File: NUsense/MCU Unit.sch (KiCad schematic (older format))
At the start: 45 parts, among them SW301 SW_Push, U301 STM32F746ZGT6, X301 24MHz, X302 ST3215SB32768H5

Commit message: pwm
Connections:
- net GPIO_9: now also U301.128 (PG13); no longer U301.124 (PG9)
- net MPU_INT: now also U301.12 (PF2); no longer U301.139 (PB8)
- net MPU_SCL: now also U301.10 (PF0); no longer U301.136 (PB6)
- net MPU_SDA/SDI: now also U301.11 (PF1); no longer U301.137 (PB7)
- net USART1_RX: now also U301.137 (PB7); no longer U301.102 (PA10)
- net USART1_TX: now also U301.136 (PB6); no longer U301.101 (PA9)
- net USART6_EN: now also U301.118 (PD4); no longer U301.98 (PC8)
- net USART6_RX: now also U301.124 (PG9); no longer U301.97 (PC7)
- net USART6_TX: now also U301.129 (PG14); no longer U301.96 (PC6)
- net TIM1_CH1: now reaches U301.100 (PA8)
- new net TIM1_CH2: U301.101 (PA9)
- new net TIM1_CH3: U301.102 (PA10)
- new net TIM8_CH1: U301.96 (PC6)
- new net TIM8_CH2: U301.97 (PC7)
- new net TIM8_CH3: U301.98 (PC8)
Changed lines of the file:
@@
 	0    -1   -1   0
 $EndComp
-Text HLabel 5150 4800 0    60   Input ~ 0
+Text HLabel 12300 5900 0    60   Input ~ 0
 MPU_INT
-Text HLabel 5150 4700 0    60   Input ~ 0
+Text HLabel 12300 5800 0    60   Input ~ 0
 MPU_SDA/SDI
-Text HLabel 5150 4600 0    60   Input ~ 0
+Text HLabel 12300 5700 0    60   Input ~ 0
 MPU_SCL
 Text HLabel 3250 7700 0    60   Input ~ 0
@@
 Text HLabel 5150 3600 0    60   BiDi ~ 0
 JTMS_SWDIO
-Text HLabel 5150 3200 0    60   Output ~ 0
+Text HLabel 5150 4600 0    60   Output ~ 0
 USART1_TX
-Text HLabel 5150 3300 0    60   Input ~ 0
+Text HLabel 5150 4700 0    60   Input ~ 0
 USART1_RX
-Text HLabel 6650 2900 2    60   Output ~ 0
+Text HLabel 13800 3700 2    60   Output ~ 0
 USART6_TX
-Text HLabel 6650 3000 2    60   Input ~ 0
+Text HLabel 13800 3200 2    60   Input ~ 0
 USART6_RX
 Text HLabel 6650 3400 2    60   Input ~ 0
@@
 Text HLabel 12300 3400 0    60   BiDi ~ 0
 VS_ALERT
-Text HLabel 6650 3100 2    60   Output ~ 0
+Text HLabel 12300 2700 0    60   Output ~ 0
 USART6_EN
 Text HLabel 12300 3000 0    60   Output ~ 0
@@
 Text HLabel 13800 3100 2    60   BiDi ~ 0
 GPIO_8
-Text HLabel 13800 3200 2    60   BiDi ~ 0
+Text HLabel 13800 3600 2    60   BiDi ~ 0
 GPIO_9
 Text HLabel 13800 3300 2    60   BiDi ~ 0
@@
 Text HLabel 13800 3500 2    60   BiDi ~ 0
 GPIO_12
+Text HLabel 5150 3100 0    60   Output ~ 0
+TIM1_CH1
+Text HLabel 5150 3200 0    60   Output ~ 0
+TIM1_CH2
+Text HLabel 5150 3300 0    60   Output ~ 0
+TIM1_CH3
+Text HLabel 6650 2900 2    60   Output ~ 0
+TIM8_CH1
+Text HLabel 6650 3000 2    60   Output ~ 0
+TIM8_CH2
+Text HLabel 6650 3100 2    60   Output ~ 0
+TIM8_CH3
 $EndSCHEMATC

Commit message: Cleans up some minor things
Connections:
- net labels added: USB_DATA
- net labels removed: OTG_HS_ULPI_D
- wire segments 141 -> 149
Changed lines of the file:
@@
 $EndComp
 $Comp
-L GND #PWR14
+L GND #PWR306
 U 1 1 5A6BFE16
 P 4000 6200
-F 0 "#PWR14" H 4000 5950 50  0001 C CNN
+F 0 "#PWR306" H 4000 5950 50  0001 C CNN
 F 1 "GND" H 4000 6050 50  0000 C CNN
 F 2 "" H 4000 6200 50  0001 C CNN
@@
 $EndComp
 $Comp
-L GND #PWR11
+L GND #PWR303
 U 1 1 5A6BFE38
 P 3200 6950
-F 0 "#PWR11" H 3200 6700 50  0001 C CNN
+F 0 "#PWR303" H 3200 6700 50  0001 C CNN
 F 1 "GND" H 3200 6800 50  0000 C CNN
 F 2 "" H 3200 6950 50  0001 C CNN
@@
 $EndComp
 $Comp
-L GND #PWR13
+L GND #PWR305
 U 1 1 5A6BFE45
 P 3800 7150
-F 0 "#PWR13" H 3800 6900 50  0001 C CNN
+F 0 "#PWR305" H 3800 6900 50  0001 C CNN
 F 1 "GND" H 3800 7000 50  0000 C CNN
 F 2 "" H 3800 7150 50  0001 C CNN
@@
 $EndComp
 $Comp
-L GND #PWR9
+L GND #PWR301
 U 1 1 5A6BFE4B
 P 2650 7150
-F 0 "#PWR9" H 2650 6900 50  0001 C CNN
+F 0 "#PWR301" H 2650 6900 50  0001 C CNN
 F 1 "GND" H 2650 7000 50  0000 C CNN
 F 2 "" H 2650 7150 50  0001 C CNN
@@
 $EndComp
 $Comp
-L GND #PWR16
+L GND #PWR308
 U 1 1 5A6BFE84
 P 4950 8100
-F 0 "#PWR16" H 4950 7850 50  0001 C CNN
+F 0 "#PWR308" H 4950 7850 50  0001 C CNN
 F 1 "GND" H 4950 7950 50  0000 C CNN
 F 2 "" H 4950 8100 50  0001 C CNN
@@
 $EndComp
 $Comp
-L GND #PWR21
+L GND #PWR313
 U 1 1 5A6BFE8A
 P 6700 7300
-F 0 "#PWR21" H 6700 7050 50  0001 C CNN
+F 0 "#PWR313" H 6700 7050 50  0001 C CNN
 F 1 "GND" H 6700 7150 50  0000 C CNN
 F 2 "" H 6700 7300 50  0001 C CNN
@@
 $EndComp
 $Comp
-L GND #PWR26
+L GND #PWR318
 U 1 1 5A6BFEA7
 P 8750 9450
-F 0 "#PWR26" H 8750 9200 50  0001 C CNN
+F 0 "#PWR318" H 8750 9200 50  0001 C CNN
 F 1 "GND" H 8750 9300 50  0000 C CNN
 F 2 "" H 8750 9450 50  0001 C CNN
@@
 $EndComp
 $Comp
-L GND #PWR23
+L GND #PWR315
 U 1 1 5A6BFEDA
 P 8050 10650
-F 0 "#PWR23" H 8050 10400 50  0001 C CNN
+F 0 "#PWR315" H 8050 10400 50  0001 C CNN
 F 1 "GND" H 8050 10500 50  0000 C CNN
 F 2 "" H 8050 10650 50  0001 C CNN
@@
 $EndComp
 $Comp
-L GND #PWR25
+L GND #PWR317
 U 1 1 5A6BFEE0
 P 8400 10650
-F 0 "#PWR25" H 8400 10400 50  0001 C CNN
+F 0 "#PWR317" H 8400 10400 50  0001 C CNN
 F 1 "GND" H 8400 10500 50  0000 C CNN
 F 2 "" H 8400 10650 50  0001 C CNN
@@
 $EndComp
 $Comp
-L GND #PWR27
+L GND #PWR319
 U 1 1 5A6BFEE6
 P 8750 10650
-F 0 "#PWR27" H 8750 10400 50  0001 C CNN
+F 0 "#PWR319" H 8750 10400 50  0001 C CNN
 F 1 "GND" H 8750 10500 50  0000 C CNN
 F 2 "" H 8750 10650 50  0001 C CNN
@@
 $EndComp
 $Comp
-L GND #PWR28
+L GND #PWR320
 U 1 1 5A6BFEEC
 P 9050 10650
-F 0 "#PWR28" H 9050 10400 50  0001 C CNN
+F 0 "#PWR320" H 9050 10400 50  0001 C CNN
 F 1 "GND" H 9050 10500 50  0000 C CNN
 F 2 "" H 9050 10650 50  0001 C CNN
@@
 $EndComp
 $Comp
-L GND #PWR29
+L GND #PWR321
 U 1 1 5A6BFEF3
 P 11000 9500
-F 0 "#PWR29" H 11000 9250 50  0001 C CNN
+F 0 "#PWR321" H 11000 9250 50  0001 C CNN
 F 1 "GND" H 11000 9350 50  0000 C CNN
 F 2 "" H 11000 9500 50  0001 C CNN
@@
 $EndComp
 $Comp
-L GND #PWR30
+L GND #PWR322
 U 1 1 5A6BFF00
 P 11000 10500
-F 0 "#PWR30" H 11000 10250 50  0001 C CNN
+F 0 "#PWR322" H 11000 10250 50  0001 C CNN
 F 1 "GND" H 11000 10350 50  0000 C CNN
 F 2 "" H 11000 10500 50  0001 C CNN
@@
 $EndComp
 $Comp
-L GND #PWR31
+L GND #PWR323
 U 1 1 5A6BFF06
 P 11300 10500
-F 0 "#PWR31" H 11300 10250 50  0001 C CNN
+F 0 "#PWR323" H 11300 10250 50  0001 C CNN
 F 1 "GND" H 11300 10350 50  0000 C CNN
 F 2 "" H 11300 10500 50  0001 C CNN
@@
 $EndComp
 $Comp
-L GND #PWR15
+L GND #PWR307
 U 1 1 5A6BFF68
 P 4550 10350
-F 0 "#PWR15" H 4550 10100 50  0001 C CNN
+F 0 "#PWR307" H 4550 10100 50  0001 C CNN
 F 1 "GND" H 4550 10200 50  0000 C CNN
 F 2 "" H 4550 10350 50  0001 C CNN
@@
 Wire Wire Line
 	11300 9900 11300 10100
-Text GLabel 5150 2600 0    60   Input ~ 0
-OTG_HS_ULPI_D
-Text GLabel 5150 4000 0    60   Input ~ 0
-OTG_HS_ULPI_D
-Text GLabel 5150 4100 0    60   Input ~ 0
-OTG_HS_ULPI_D
-Text GLabel 5150 4500 0    60   Input ~ 0
-OTG_HS_ULPI_D
-Text GLabel 5150 5000 0    60   Input ~ 0
-OTG_HS_ULPI_D
-Text GLabel 5150 5100 0    60   Input ~ 0
-OTG_HS_ULPI_D
-Text GLabel 5150 5200 0    60   Input ~ 0
-OTG_HS_ULPI_D
-Text GLabel 5150 5300 0    60   Input ~ 0
-OTG_HS_ULPI_D
-$Comp
-L +3.3V #PWR20
+$Comp
+L +3.3V #PWR312
 U 1 1 5A6FCDF0
 P 6700 7000
-F 0 "#PWR20" H 6700 6850 50  0001 C CNN
+F 0 "#PWR312" H 6700 6850 50  0001 C CNN
 F 1 "+3.3V" H 6700 7140 50  0000 C CNN
 F 2 "" H 6700 7000 50  0001 C CNN
@@
 $EndComp
 $Comp
-L +3.3V #PWR18
+L +3.3V #PWR310
 U 1 1 5A6FCE7A
 P 5800 7500
-F 0 "#PWR18" H 5800 7350 50  0001 C CNN
+F 0 "#PWR310" H 5800 7350 50  0001 C CNN
 F 1 "+3.3V" H 5800 7640 50  0000 C CNN
 F 2 "" H 5800 7500 50  0001 C CNN
@@
 $EndComp
 $Comp
-L +3.3V #PWR24
+L +3.3V #PWR316
 U 1 1 5A6FD2DC
 P 8250 8400
-F 0 "#PWR24" H 8250 8250 50  0001 C CNN
+F 0 "#PWR316" H 8250 8250 50  0001 C CNN
 F 1 "+3.3V" H 8250 8540 50  0000 C CNN
 F 2 "" H 8250 8400 50  0001 C CNN
@@
 VDD3o3V_MCU
 $Comp
-L GND #PWR17
+L GND #PWR309
 U 1 1 5A701246
 P 5500 9800
-F 0 "#PWR17" H 5500 9550 50  0001 C CNN
+F 0 "#PWR309" H 5500 9550 50  0001 C CNN
 F 1 "GND" H 5500 9650 50  0000 C CNN
 F 2 "" H 5500 9800 50  0001 C CNN
@@
 VDD_REF+
 $Comp
-L GND #PWR19
+L GND #PWR311
 U 1 1 5A7014A6
 P 6300 10750
-F 0 "#PWR19" H 6300 10500 50  0001 C CNN
+F 0 "#PWR311" H 6300 10500 50  0001 C CNN
 F 1 "GND" H 6300 10600 50  0000 C CNN
 F 2 "" H 6300 10750 50  0001 C CNN
@@
 	8400 9650 8400 10300
 $Comp
-L +3.3V #PWR22
+L +3.3V #PWR314
 U 1 1 5A6FD08D
 P 6900 9900
-F 0 "#PWR22" H 6900 9750 50  0001 C CNN
+F 0 "#PWR314" H 6900 9750 50  0001 C CNN
 F 1 "+3.3V" H 6900 10040 50  0000 C CNN
 F 2 "" H 6900 9900 50  0001 C CNN
@@
 $EndComp
 $Comp
-L GND #PWR10
+L GND #PWR302
 U 1 1 5A6BFE10
 P 2700 6200
-F 0 "#PWR10" H 2700 5950 50  0001 C CNN
+F 0 "#PWR302" H 2700 5950 50  0001 C CNN
 F 1 "GND" H 2700 6050 50  0000 C CNN
 F 2 "" H 2700 6200 50  0001 C CNN
@@
 	5150 5800 4600 5800
 $Comp
-L GND #PWR12
+L GND #PWR304
 U 1 1 5A7647F9
 P 3400 6450
-F 0 "#PWR12" H 3400 6200 50  0001 C CNN
+F 0 "#PWR304" H 3400 6200 50  0001 C CNN
 F 1 "GND" H 3400 6300 50  0000 C CNN
 F 2 "" H 3400 6450 50  0001 C CNN
@@
 Text HLabel 6650 3100 2    60   Output ~ 0
 TIM8_CH3
+Entry Bus Bus
+	4200 2500 4300 2600
+Entry Bus Bus
+	4200 3900 4300 4000
+Entry Bus Bus
+	4200 4000 4300 4100
+Entry Bus Bus
+	4200 4400 4300 4500
+Entry Bus Bus
+	4200 4900 4300 5000
+Entry Bus Bus
+	4200 5000 4300 5100
+Entry Bus Bus
+	4200 5100 4300 5200
+Entry Bus Bus
+	4200 5200 4300 5300
+Wire Bus Line
+	4200 5200 4200 2400
+Wire Bus Line
+	4200 2400 3950 2400
+Text HLabel 3950 2400 0    60   BiDi ~ 0
+USB_DATA
+Wire Wire Line
+	5150 5300 4300 5300
+Wire Wire Line
+	5150 5200 4300 5200
+Wire Wire Line
+	5150 5100 4300 5100
+Wire Wire Line
+	5150 5000 4300 5000
+Wire Wire Line
+	5150 4500 4300 4500
+Wire Wire Line
+	5150 4100 4300 4100
+Wire Wire Line
+	5150 4000 4300 4000
+Wire Wire Line
+	4300 2600 5150 2600
 $EndSCHEMATC

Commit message: Further Cleaning
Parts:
- added C335: 0.1uF, Capacitors_SMD:C_0805_HandSoldering, symbol C
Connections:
- net labels removed: RTC_BAT, VDD3o3V_MCU, VDD_REF+
- wire segments 149 -> 152
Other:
- note added: "RTC Battery Input"
- moved on the sheet: C324, C325, C326, C327

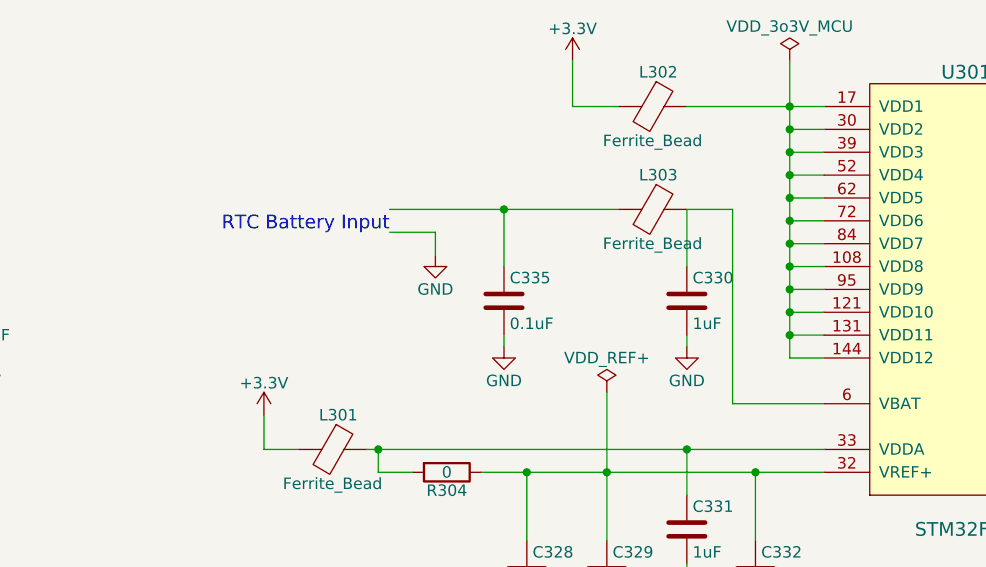
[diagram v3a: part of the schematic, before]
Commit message: RTC removed
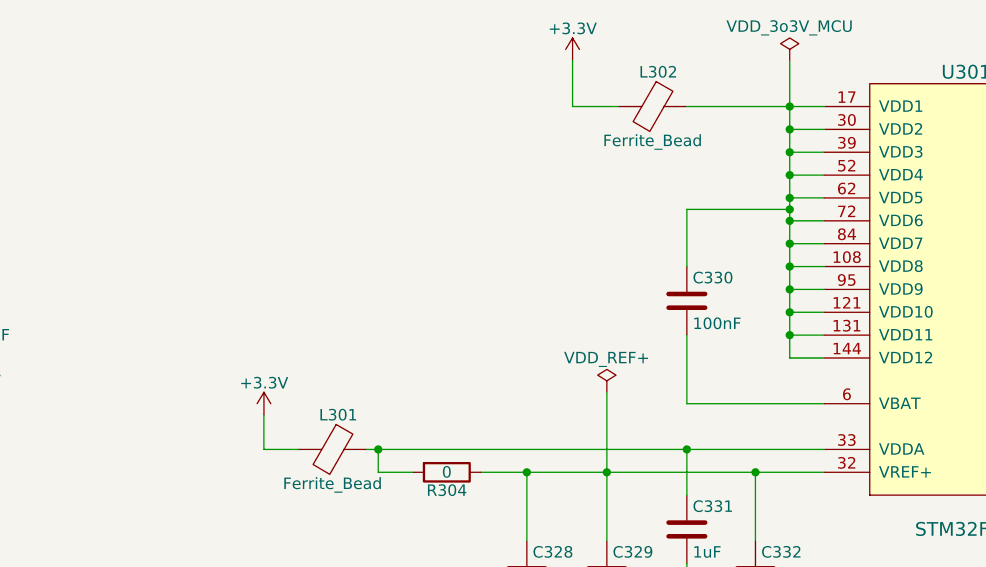
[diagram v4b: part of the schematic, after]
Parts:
- removed C335: 0.1uF, Capacitors_SMD:C_0805_HandSoldering, symbol C
- removed L303: Ferrite_Bead, symbol Ferrite_Bead
- C330: value 1uF -> 100nF
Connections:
- wire segments 152 -> 146
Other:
- note removed: "RTC Battery Input"
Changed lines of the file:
@@
-$EndComp
-$Comp
-L Ferrite_Bead L303
-U 1 1 5A6BFE99
-P 8600 8850
-F 0 "L303" V 8450 8875 50  0000 C CNN
-F 1 "Ferrite_Bead" V 8750 8850 50  0000 C CNN
-F 2 "" V 8530 8850 50  0001 C CNN
-F 3 "" H 8600 8850 50  0001 C CNN
-	1    8600 8850
-	0    1    1    0
 $EndComp
 $Comp
@@
 P 8750 9250
 F 0 "C330" H 8775 9350 50  0000 L CNN
-F 1 "1uF" H 8775 9150 50  0000 L CNN
+F 1 "100nF" H 8775 9150 50  0000 L CNN
 F 2 "Capacitors_SMD:C_0805_HandSoldering" H 8788 9100 50  0001 C CNN
 F 3 "" H 8750 9250 50  0001 C CNN
 	1    8750 9250
-	1    0    0    -1
-$EndComp
-$Comp
-L GND #PWR318
-U 1 1 5A6BFEA7
-P 8750 9450
-F 0 "#PWR318" H 8750 9200 50  0001 C CNN
-F 1 "GND" H 8750 9300 50  0000 C CNN
-F 2 "" H 8750 9450 50  0001 C CNN
-F 3 "" H 8750 9450 50  0001 C CNN
-	1    8750 9450
 	1    0    0    -1
 $EndComp
@@
 	8750 8850 8750 9100
 Wire Wire Line
-	8750 9400 8750 9450
-Wire Wire Line
-	8750 8850 8950 8850
-Wire Wire Line
-	8950 8850 8950 9700
-Wire Wire Line
-	8950 9700 9350 9700
+	8750 9400 8750 9700
+Wire Wire Line
+	8750 8850 9200 8850
+Wire Wire Line
+	8750 9700 9350 9700
 Wire Wire Line
 	8250 8400 8450 8400
-Wire Wire Line
-	7450 8850 8450 8850
 Wire Wire Line
 	7850 10000 9350 10000
@@
 	1    0    0    -1
 $EndComp
-$Comp
-L C C335
-U 1 1 5A79B3A0
-P 7950 9250
-F 0 "C335" H 7975 9350 50  0000 L CNN
-F 1 "0.1uF" H 7975 9150 50  0000 L CNN
-F 2 "Capacitors_SMD:C_0805_HandSoldering" H 7988 9100 50  0001 C CNN
-F 3 "" H 7950 9250 50  0001 C CNN
-	1    7950 9250
-	1    0    0    -1
-$EndComp
-$Comp
-L GND #PWR?
-U 1 1 5A79B44A
-P 7950 9450
-F 0 "#PWR?" H 7950 9200 50  0001 C CNN
-F 1 "GND" H 7950 9300 50  0000 C CNN
-F 2 "" H 7950 9450 50  0001 C CNN
-F 3 "" H 7950 9450 50  0001 C CNN
-	1    7950 9450
-	1    0    0    -1
-$EndComp
-Wire Wire Line
-	7950 9400 7950 9450
-Wire Wire Line
-	7950 9100 7950 8850
-Connection ~ 7950 8850
-Wire Wire Line
-	7450 8950 7650 8950
-Wire Wire Line
-	7650 8950 7650 9050
-$Comp
-L GND #PWR?
-U 1 1 5A79BA38
-P 7650 9050
-F 0 "#PWR?" H 7650 8800 50  0001 C CNN
-F 1 "GND" H 7650 8900 50  0000 C CNN
-F 2 "" H 7650 9050 50  0001 C CNN
-F 3 "" H 7650 9050 50  0001 C CNN
-	1    7650 9050
-	1    0    0    -1
-$EndComp
-Text Notes 7450 8950 2    60   ~ 0
-RTC Battery Input
+Connection ~ 9200 8850
 $EndSCHEMATC

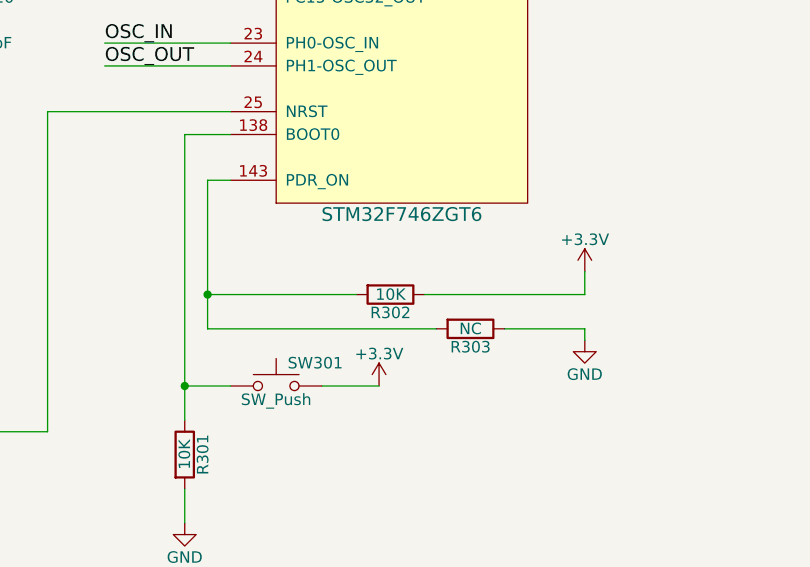
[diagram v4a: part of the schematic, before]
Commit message: Add labels
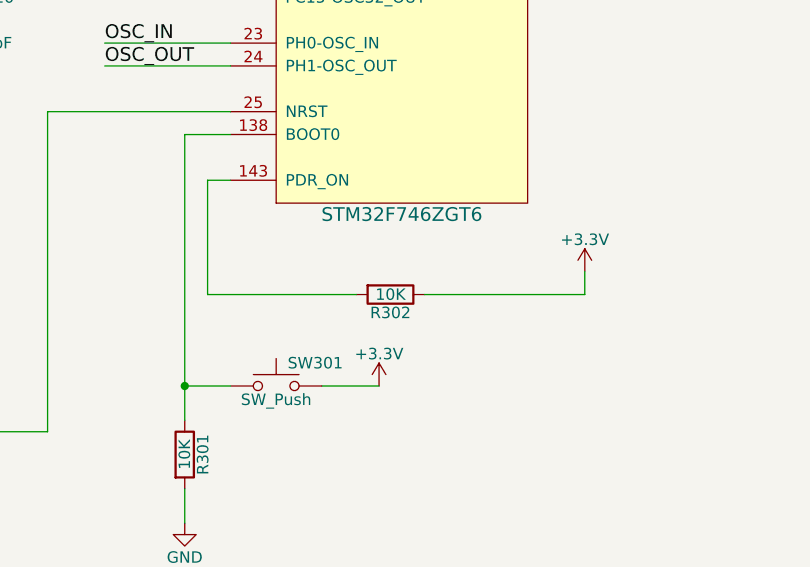
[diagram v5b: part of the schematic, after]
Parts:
- removed R303: NC, Resistors_SMD:R_0805_HandSoldering, symbol R
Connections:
- wire segments 146 -> 143
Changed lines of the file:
@@
-$EndComp
-$Comp
-L R R303
-U 1 1 5A6BFE6E
-P 6200 7250
-F 0 "R303" V 6280 7250 50  0000 C CNN
-F 1 "NC" V 6200 7250 50  0000 C CNN
-F 2 "Resistors_SMD:R_0805_HandSoldering" V 6130 7250 50  0001 C CNN
-F 3 "" H 6200 7250 50  0001 C CNN
-	1    6200 7250
-	0    1    1    0
 $EndComp
 $Comp
@@
 F 3 "" H 4950 8100 50  0001 C CNN
 	1    4950 8100
-	1    0    0    -1
-$EndComp
-$Comp
-L GND #PWR313
-U 1 1 5A6BFE8A
-P 6700 7300
-F 0 "#PWR313" H 6700 7050 50  0001 C CNN
-F 1 "GND" H 6700 7150 50  0000 C CNN
-F 2 "" H 6700 7300 50  0001 C CNN
-F 3 "" H 6700 7300 50  0001 C CNN
-	1    6700 7300
 	1    0    0    -1
 $EndComp
@@
 	5700 7100 5050 7100
 Wire Wire Line
-	5050 6600 5050 7250
-Wire Wire Line
 	5050 6600 5150 6600
-Wire Wire Line
-	5050 7250 6050 7250
-Connection ~ 5050 7100
 Wire Wire Line
 	4950 6400 4950 7650
@@
 Wire Wire Line
 	6000 7100 6700 7100
-Wire Wire Line
-	6350 7250 6700 7250
-Wire Wire Line
-	6700 7250 6700 7300
 Wire Wire Line
 	8750 8400 9350 8400
@@
 $EndComp
 Connection ~ 9200 8850
+Wire Wire Line
+	5050 7100 5050 6600
 $EndSCHEMATC
